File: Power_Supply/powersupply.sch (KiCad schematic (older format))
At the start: 80 parts, among them J1 1x2, J101 USB_B_Micro, J102 Conn_01x03_Male, J103 Default_Jumper, J104 Default_Jumper, J2 1x2, Q1 IRF9Z24NPBF, SW1 KMR2, SW2 joystick-K1-1506DN-01, U101 AZ1117E-3.3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

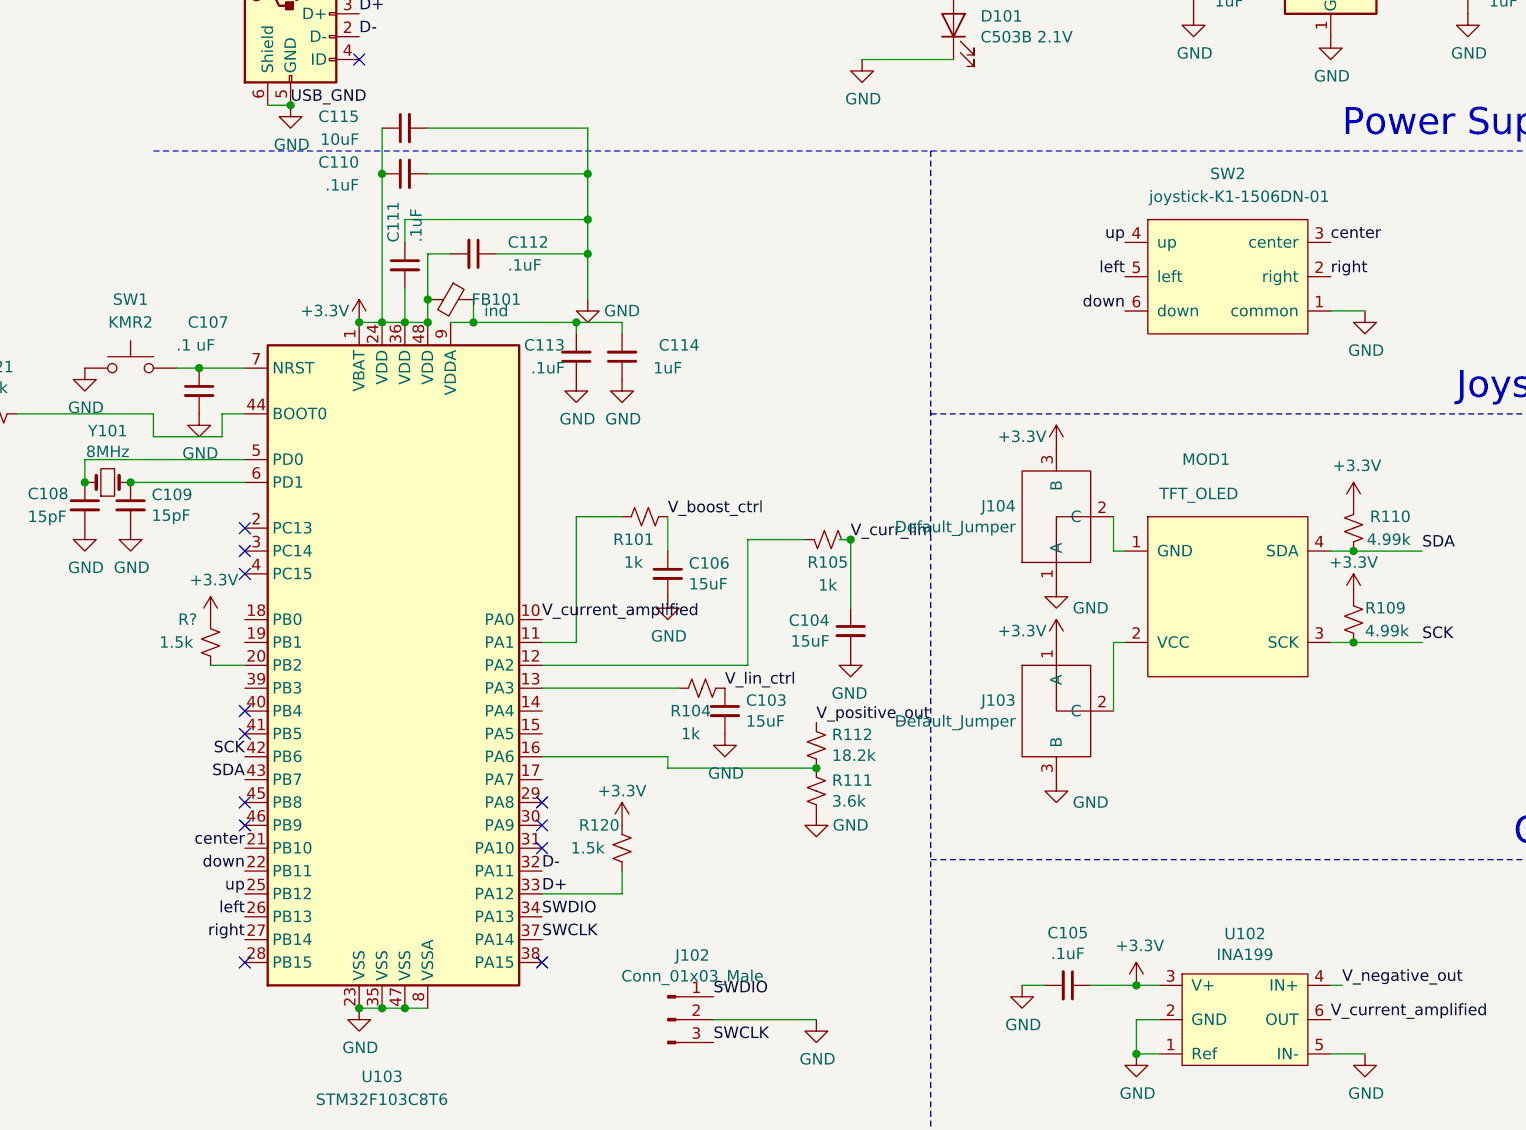
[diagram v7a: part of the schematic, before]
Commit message: Fixed directional button (for real this time?)
Also laid out pullup resistor to make bootloader happy.
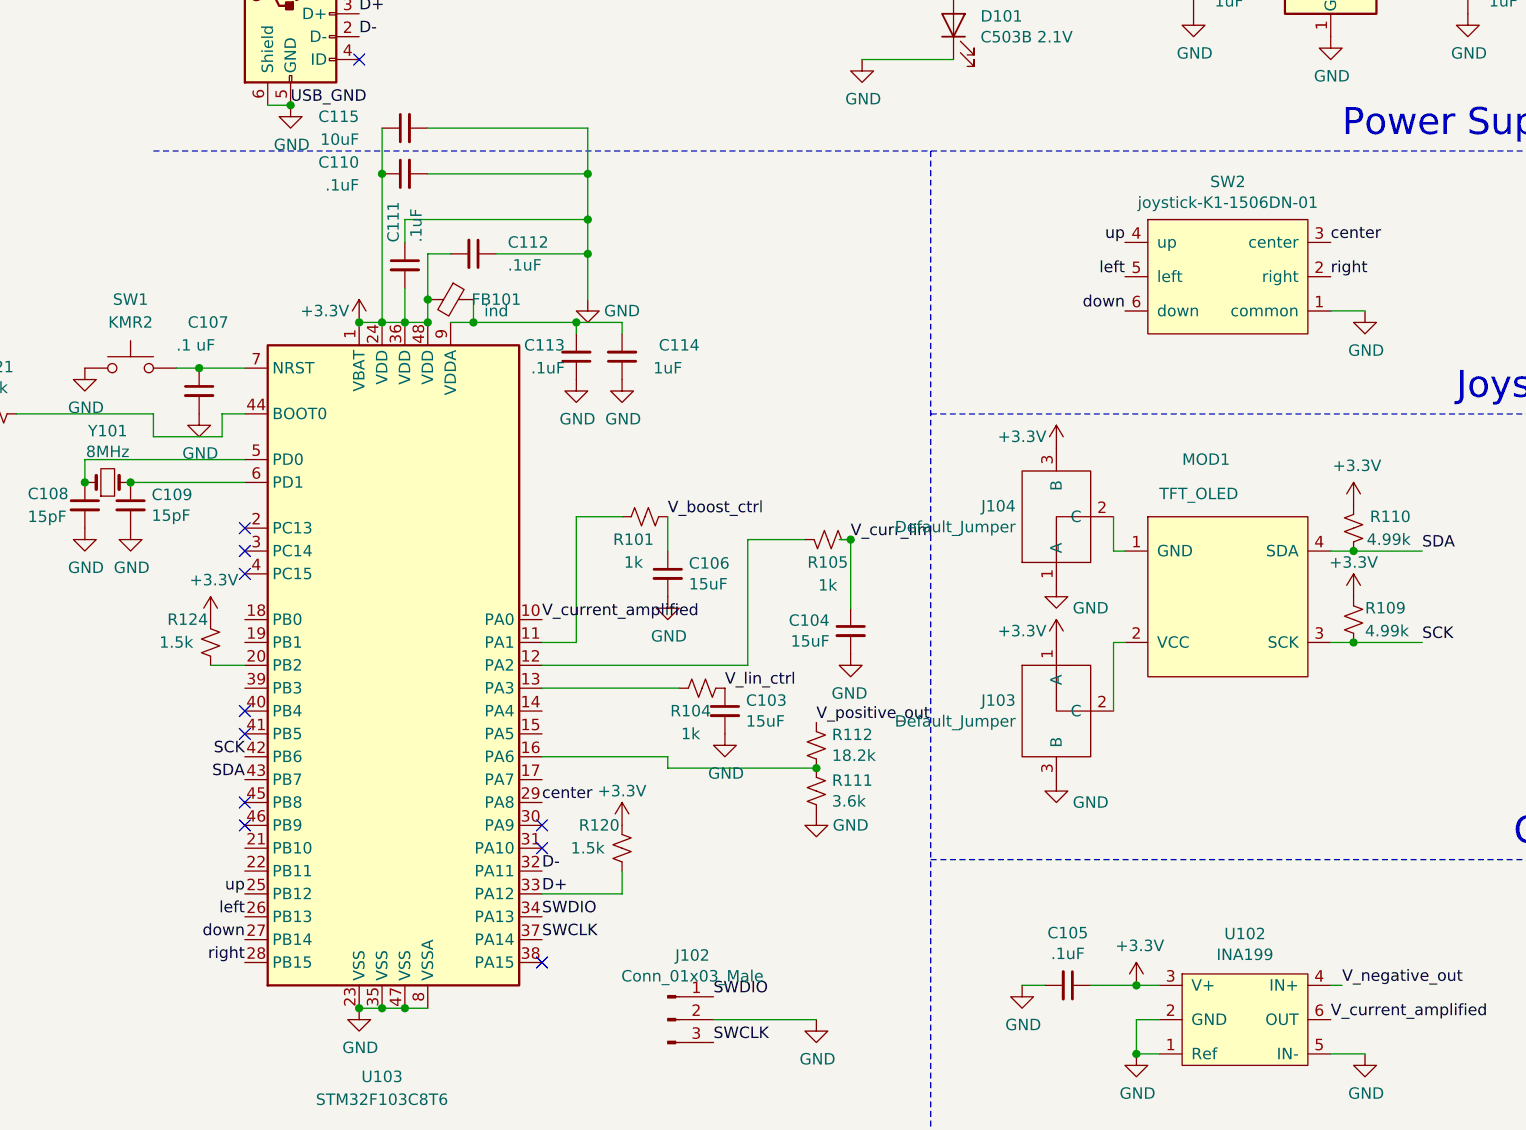
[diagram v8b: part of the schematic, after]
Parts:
- gave numbers to parts that had none: 1
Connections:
- net center: now also U103.29 (PA8); no longer U103.21 (PB10)
- net down: now also U103.27 (PB14); no longer U103.22 (PB11)
- net right: now also U103.28 (PB15); no longer U103.27 (PB14)
- no-connect marks 18 -> 16
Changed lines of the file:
@@
 EESchema Schematic File Version 4
 LIBS:powersupply-cache
-EELAYER 30 0
+EELAYER 26 0
 EELAYER END
 $Descr A4 11693 8268
@@
 	1    9600 3750
 	1    0    0    1
-$EndComp
-$Comp
-L powersupply:joystick-K1-1506DN-01 SW2
-U 1 1 5D4C0110
-P 5150 1950
-F 0 "SW2" H 5150 1950 50  0000 C CNN
-F 1 "joystick-K1-1506DN-01" H 5200 1850 50  0000 C CNN
-F 2 "powersupply:directional_switch_10mm" H 5150 1950 50  0001 C CNN
-F 3 "" H 5150 1950 50  0001 C CNN
-	1    5150 1950
-	1    0    0    -1
 $EndComp
 Text Label 4700 2250 2    50   ~ 0
@@
 NoConn ~ 850  4700
 NoConn ~ 850  4800
-NoConn ~ 850  5400
-NoConn ~ 2150 4700
 NoConn ~ 2150 4800
 NoConn ~ 2150 4900
@@
 	1    0    0    -1
 $EndComp
-Text Label 850  4900 2    50   ~ 0
+Text Label 2150 4700 0    50   ~ 0
 center
-Text Label 850  5000 2    50   ~ 0
+Text Label 850  5300 2    50   ~ 0
 down
 Text Label 850  5100 2    50   ~ 0
@@
 Text Label 850  5200 2    50   ~ 0
 left
-Text Label 850  5300 2    50   ~ 0
+Text Label 850  5400 2    50   ~ 0
 right
 Text Label 850  4600 2    50   ~ 0
@@
 NoConn ~ 5050 7500
 $Comp
-L Device:R_Small_US R?
+L Device:R_Small_US R124
 U 1 1 5DC15C01
 P 700 4000
-F 0 "R?" H 600 4100 50  0000 C CNN
+F 0 "R124" H 600 4100 50  0000 C CNN
 F 1 "1.5k" H 550 4000 50  0000 C CNN
 F 2 "Resistor_SMD:R_0805_2012Metric" H 700 4000 50  0001 C CNN
@@
 	700  4100 850  4100
 $Comp
-L power:+3.3V #PWR?
+L power:+3.3V #PWR0145
 U 1 1 5DC39F86
 P 700 3900
-F 0 "#PWR?" H 700 3750 50  0001 C CNN
+F 0 "#PWR0145" H 700 3750 50  0001 C CNN
 F 1 "+3.3V" H 715 4073 50  0000 C CNN
 F 2 "" H 700 3900 50  0001 C CNN
@@
 	1    0    0    -1
 $EndComp
+$Comp
+L powersupply:joystick-K1-1506DN-01 SW2
+U 1 1 5DCEFD6A
+P 5150 1950
+F 0 "SW2" H 5150 1915 50  0000 C CNN
+F 1 "joystick-K1-1506DN-01" H 5150 1824 50  0000 C CNN
+F 2 "powersupply:directional_switch_10mm" H 5150 1950 50  0001 C CNN
+F 3 "" H 5150 1950 50  0001 C CNN
+	1    5150 1950
+	1    0    0    -1
+$EndComp
